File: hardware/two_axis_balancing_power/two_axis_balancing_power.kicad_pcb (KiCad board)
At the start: 4 copper layers, 50 x 42.9 mm, 39 parts, among them J1 Conn_01x02, J2 Conn_02x05, J3 Conn_01x02, Q1 AO3401A, U1 RPL-1.0-R, U2 LM393, U3 TB6612FNG

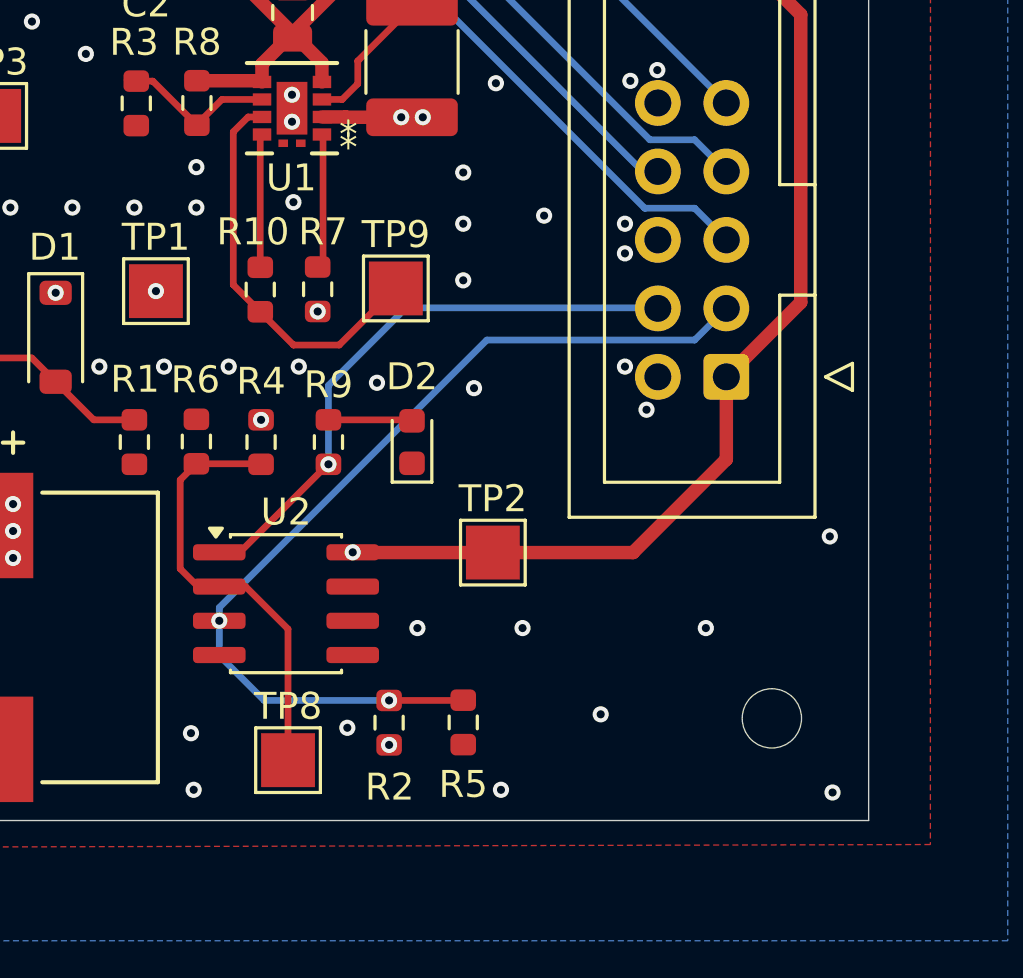
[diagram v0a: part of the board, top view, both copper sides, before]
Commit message: Fixed issue with battery monitoring functionality
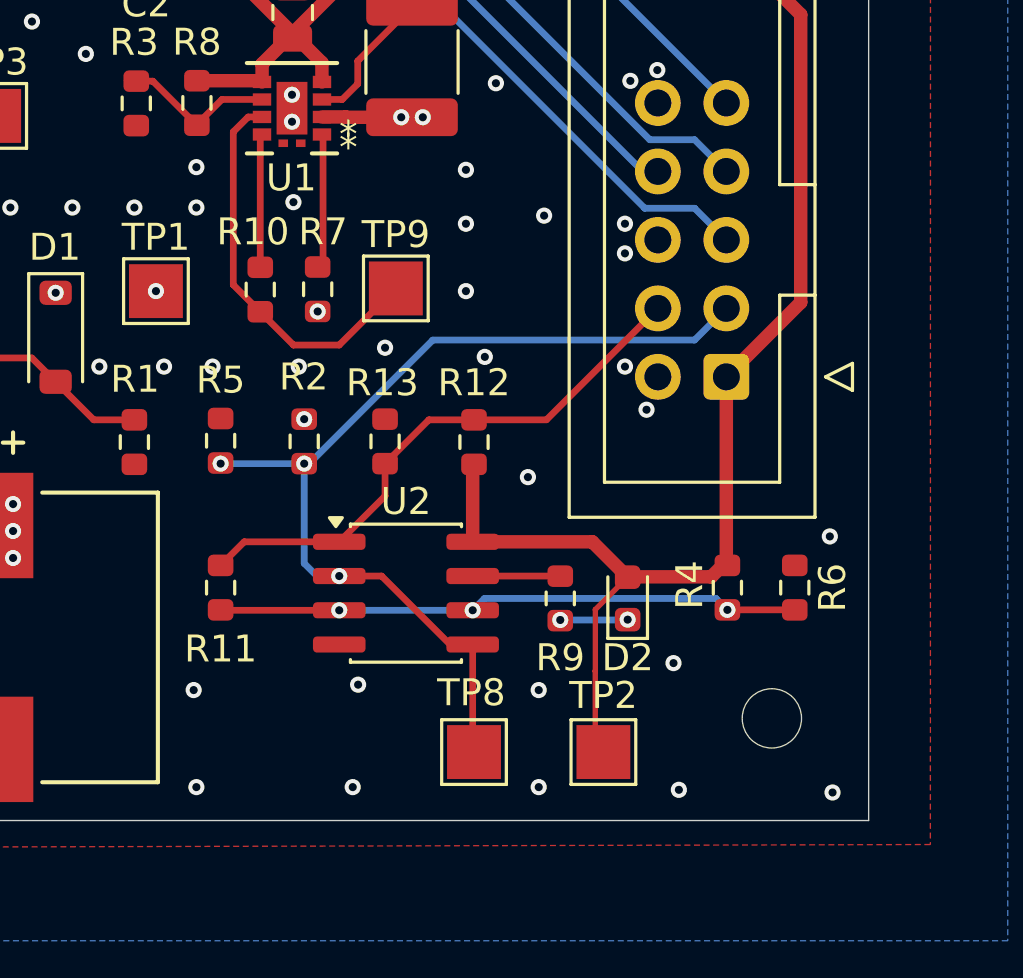
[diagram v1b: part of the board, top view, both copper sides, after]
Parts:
- added R11: 220kR, Resistor_SMD:R_0603_1608Metric, F.Cu at (153.8, 117.9)
- added R12: 10kR, Resistor_SMD:R_0603_1608Metric, F.Cu at (163.2, 112.5)
- added R13: 15kR, Resistor_SMD:R_0603_1608Metric, F.Cu at (159.9, 112.5)
- R9: value 220R -> 470R
- moved R6 22.9 mm to (175.1, 117.9)
- moved R4 18.1 mm to (172.6, 117.9), turned to -90 degrees
- moved R5 13.8 mm to (153.8, 112.5)
- moved R2 10.9 mm to (156.9, 112.5), turned to 90 degrees
- moved R9 10.4 mm to (166.4, 118.3), turned to 90 degrees
- moved D2 9.88 mm to (168.9, 118.3)
- moved TP2 8.46 mm to (168.0, 124.0)
- moved TP8 6.91 mm to (163.2, 124.0)
- moved U2 4.47 mm to (160.7, 118.1)
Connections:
- D2 pad 1: GND -> Net-(D2-K)
- D2 pad 2: Net-(D2-A) -> +5V
- R4 pad 1: /BAT_REF -> +5V
- R4 pad 2: +5V -> Net-(U2A-+)
- R5 pad 1: /BAT_LEV -> GND
- R5 pad 2: GND -> /BAT_LEV
- R6 pad 1: /BAT_REF -> Net-(U2A-+)
- R9 pad 1: Net-(D2-A) -> Net-(D2-K)
- R9 pad 2: /BAT_LOW -> Net-(R9-Pad2)
- TP8 pad 1: /BAT_REF -> /BAT_LEV
- U2 pad 2: /BAT_REF -> /BAT_LEV
- U2 pad 3: /BAT_LEV -> Net-(U2A-+)
- U2 pad 5: unconnected-(U2B-+-Pad5) -> /BAT_LEV
- U2 pad 6: unconnected-(U2B---Pad6) -> Net-(U2A-+)
- U2 pad 7: unconnected-(U2-Pad7) -> Net-(R9-Pad2)
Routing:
- net Net-(U2A-+): track 0.00 -> 21.7 mm, vias 0 -> 3
- net /BAT_REF: track 16.4 -> 0.00 mm
- net VBAT: track 19.0 -> 7.89 mm
- net Net-(R9-Pad2): track 0.00 -> 3.25 mm
- net Net-(D2-A): track 3.12 -> 0.00 mm
- net Net-(D2-K): track 0.00 -> 2.53 mm, vias 0 -> 2
- net +5V: track 81.3 -> 83.6 mm, vias 2 -> 0
- net /BAT_LEV: track 34.9 -> 36.4 mm, vias 2 -> 3
- net /BAT_LOW: track 21.8 -> 20.9 mm, vias 1 -> 0
- net GND: vias 80 -> 81
